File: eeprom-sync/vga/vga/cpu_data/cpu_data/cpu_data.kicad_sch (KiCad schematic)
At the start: 39 parts, among them J1 Conn_02x06_Odd_Even, J10 Conn_01x03_Female, J12 Conn_02x05_Odd_Even, J2 Conn_01x04_Male, J3 Conn_01x04_Female, J4 Conn_01x15_Female, J5 Conn_01x15_Female, J6 Conn_01x08_Female, J7 Conn_02x04_Odd_Even, J8 Conn_02x08_Odd_Even, J9 Conn_01x08_Female, Q1 Q_NMOS_GSD, U1 GAL22V10, U2 74HC14, U3 74LS02, U4 IDT7205L12JG, U5 74LS573

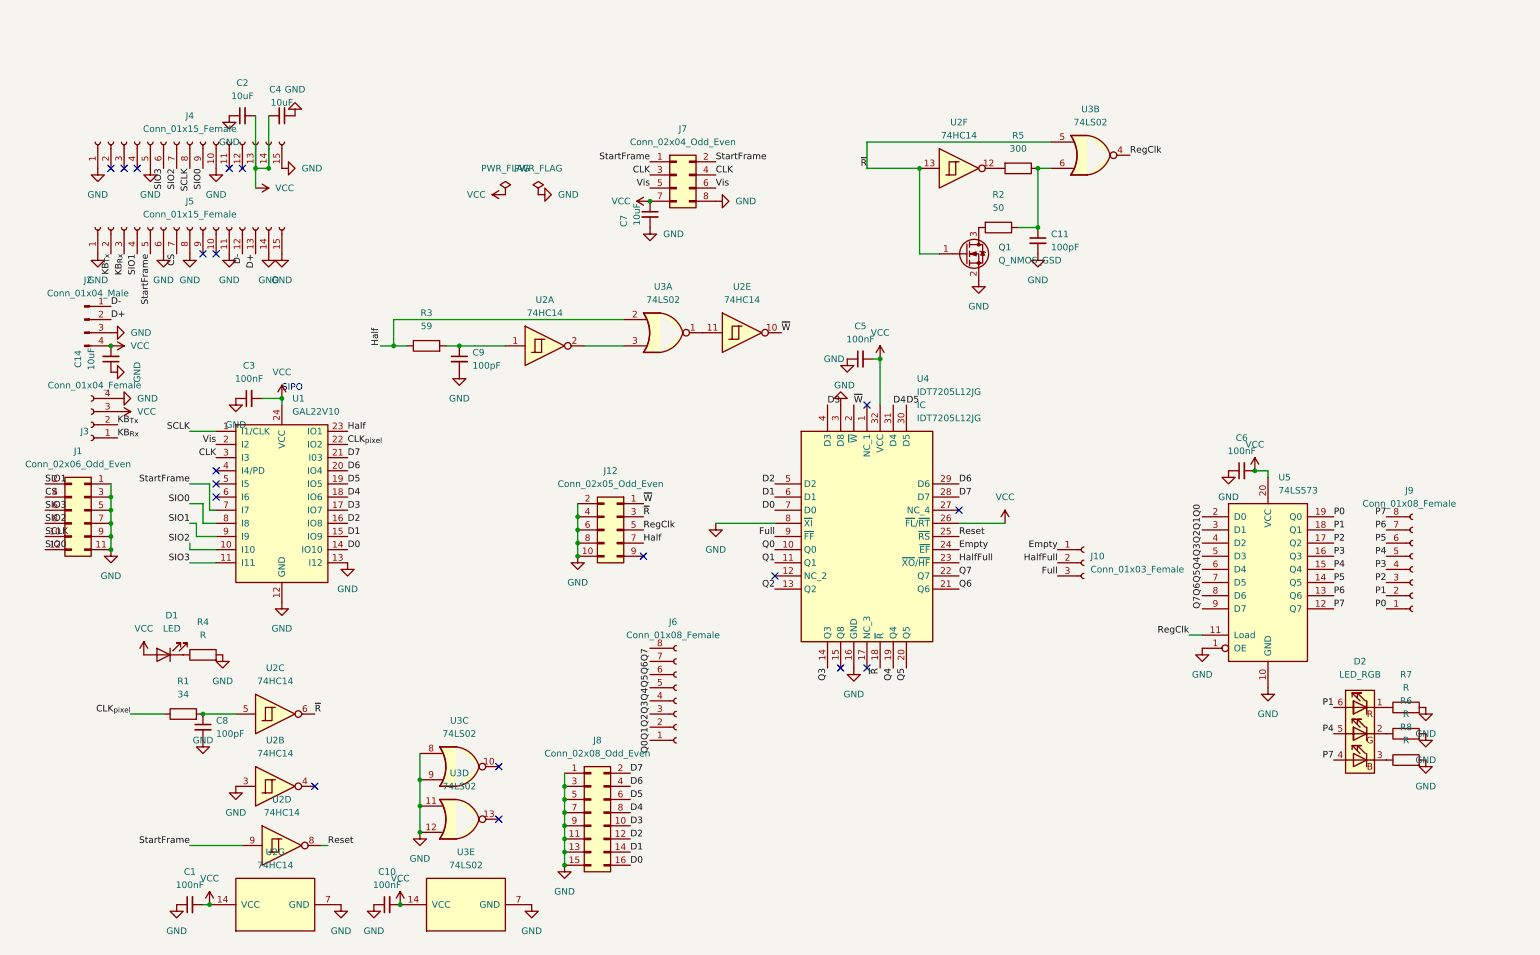
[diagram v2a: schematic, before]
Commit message: updating board to use clocked latches as the data mile markers instead of RC time circuits. Also adding a clock board breadboardable circuit module
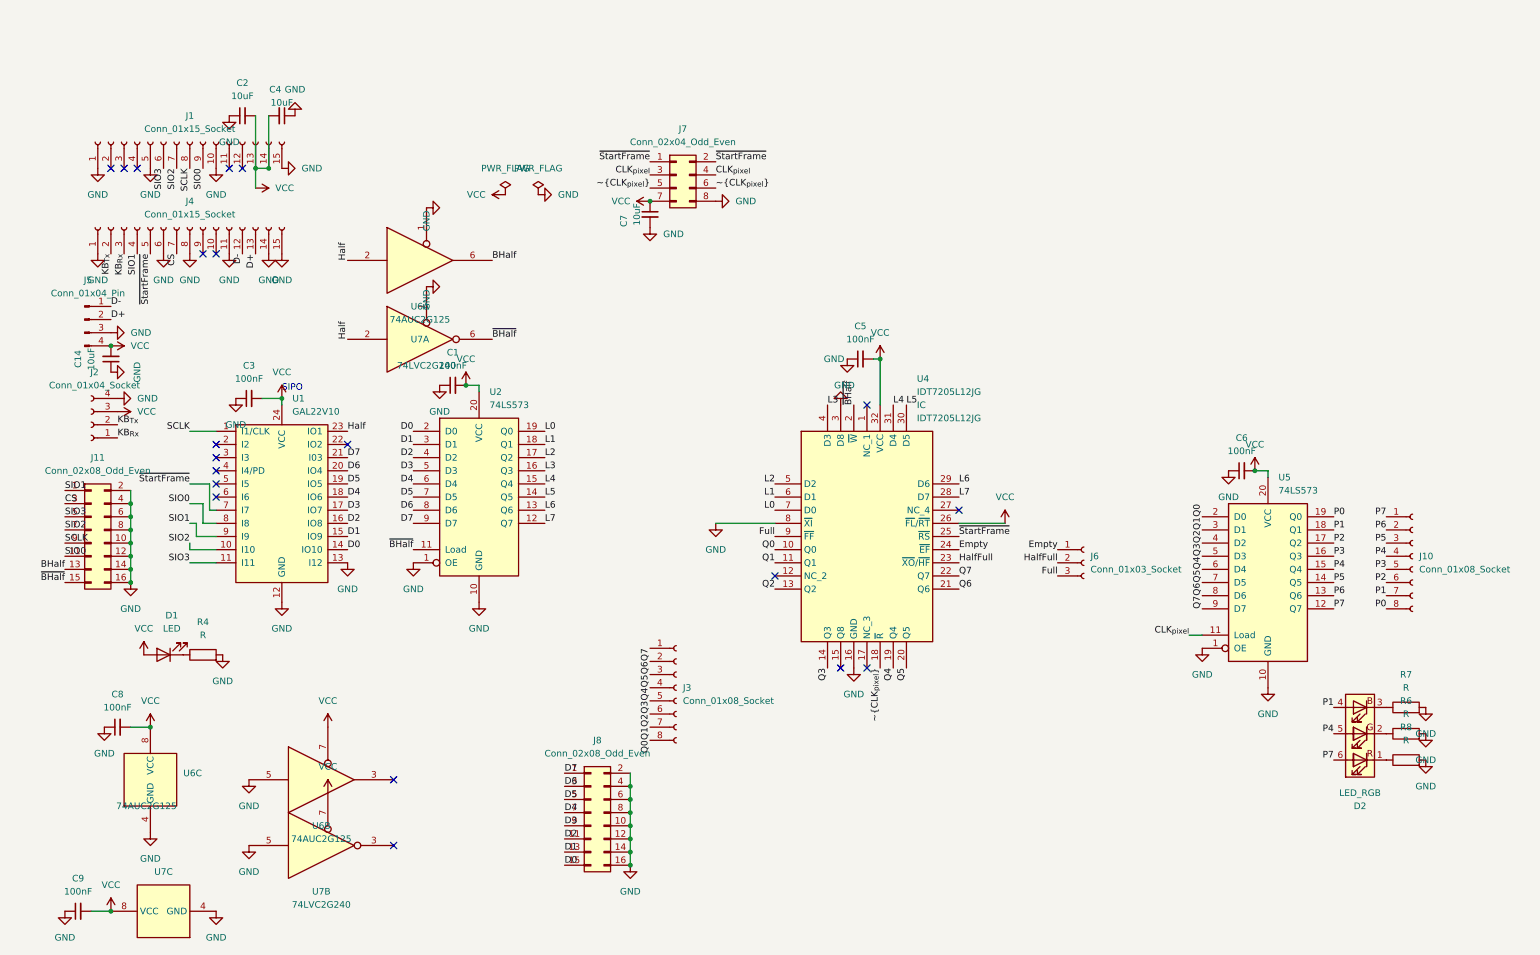
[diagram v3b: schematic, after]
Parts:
- removed C10: 100nF, Capacitor_SMD:C_0805_2012Metric_Pad1.18x1.45mm_HandSolder, symbol Device:C_Small
- removed C11: 100pF, Capacitor_SMD:C_0805_2012Metric_Pad1.18x1.45mm_HandSolder, symbol Device:C_Small
- removed J1: Conn_02x06_Odd_Even, Connector_PinHeader_2.54mm:PinHeader_2x06_P2.54mm_Vertical, symbol Connector_Generic:Conn_02x06_Odd_Even
- removed J10: Conn_01x03_Female, Connector_PinSocket_2.54mm:PinSocket_1x03_P2.54mm_Vertical, symbol Connector:Conn_01x03_Female
- removed J12: Conn_02x05_Odd_Even, Connector_PinHeader_2.54mm:PinHeader_2x05_P2.54mm_Vertical, symbol Connector_Generic:Conn_02x05_Odd_Even
- removed J2: Conn_01x04_Male, Connector_PinHeader_2.54mm:PinHeader_1x04_P2.54mm_Vertical, symbol Connector:Conn_01x04_Male
- removed J3: Conn_01x04_Female, Connector_PinSocket_2.54mm:PinSocket_1x04_P2.54mm_Vertical, symbol Connector:Conn_01x04_Female
- removed J4, J5: Conn_01x15_Female, Connector_PinSocket_2.54mm:PinSocket_1x15_P2.54mm_Vertical, symbol Connector:Conn_01x15_Female
- removed J6, J9: Conn_01x08_Female, Connector_PinSocket_2.54mm:PinSocket_1x08_P2.54mm_Vertical, symbol Connector:Conn_01x08_Female
- removed Q1: Q_NMOS_GSD, Package_TO_SOT_SMD:SOT-323_SC-70_Handsoldering, symbol Device:Q_NMOS_GSD
- removed R1: 34, Resistor_SMD:R_0805_2012Metric_Pad1.20x1.40mm_HandSolder, symbol Device:R
- removed R2: 50, Resistor_SMD:R_0805_2012Metric_Pad1.20x1.40mm_HandSolder, symbol Device:R
- removed R3: 59, Resistor_SMD:R_0805_2012Metric_Pad1.20x1.40mm_HandSolder, symbol Device:R
- removed R5: 300, Resistor_SMD:R_0805_2012Metric_Pad1.20x1.40mm_HandSolder, symbol Device:R
- removed U2: 74HC14, Package_SO:SOIC-14_3.9x8.7mm_P1.27mm, symbol 74xx:74HC14
- removed U3: 74LS02, Package_SO:SOIC-14_3.9x8.7mm_P1.27mm, symbol 74xx:74LS02
- added J1, J4: Conn_01x15_Socket, Connector_PinSocket_2.54mm:PinSocket_1x15_P2.54mm_Vertical, symbol Connector:Conn_01x15_Socket
- added J10: Conn_01x08_Socket, Connector_PinSocket_2.54mm:PinSocket_1x08_P2.54mm_Vertical, symbol Connector:Conn_01x08_Socket
- added J11: Conn_02x08_Odd_Even, Connector_PinHeader_2.54mm:PinHeader_2x08_P2.54mm_Vertical, symbol Connector_Generic:Conn_02x08_Odd_Even
- added J2: Conn_01x04_Socket, Connector_PinSocket_2.54mm:PinSocket_1x04_P2.54mm_Vertical, symbol Connector:Conn_01x04_Socket
- added J3: Conn_01x08_Socket, Connector_PinHeader_2.54mm:PinHeader_1x08_P2.54mm_Vertical, symbol Connector:Conn_01x08_Socket
- added J5: Conn_01x04_Pin, Connector_PinHeader_2.54mm:PinHeader_1x04_P2.54mm_Vertical, symbol Connector:Conn_01x04_Pin
- added J6: Conn_01x03_Socket, Connector_PinSocket_2.54mm:PinSocket_1x03_P2.54mm_Vertical, symbol Connector:Conn_01x03_Socket
- added U2: 74LS573, Package_SO:SOIC-20W_7.5x15.4mm_P1.27mm, symbol 74xx:74LS573
- added U6: 74AUC2G125, Package_SO:TSSOP-8_3x3mm_P0.65mm, symbol 74xGxx:74AUC2G125
- added U7: 74LVC2G240, Package_SO:TSSOP-8_3x3mm_P0.65mm, symbol 74xGxx:74LVC2G240
- C1: footprint Capacitor_SMD:C_0805_2012Metric_Pad1.18x1.45mm_HandSolder -> plcc32:plcc32-socket; Pruduct (none) -> https://www.mouser.com/ProductDetail/Samsung-Electro-Mechan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
- C8: value 100pF -> 100nF
- C9: value 100pF -> 100nF; Product https://www.mouser.com/ProductDetail/Samsung-Electro-Mechan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 -> (none)
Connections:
- net RegClk is gone; now on net CLK_{pixel}: U5.11 (Load)
- net StartFrame is gone; now on net ~{StartFrame}: J7.1 (Pin_1), J7.2 (Pin_2), U1.7 (I7)
- net ~{R} is gone; now on net ~{CLK_{pixel}}: U4.18 (~{R})
- net CLK_{pixel}: now also J7.3 (Pin_3), J7.4 (Pin_4); no longer U1.22 (IO2)
- net CS: now also J11.3 (Pin_3), J4.7 (Pin_7)
- net D+: now also J4.13 (Pin_13), J5.2 (Pin_2)
- net D-: now also J4.12 (Pin_12), J5.1 (Pin_1)
- net D0: now also J8.15 (Pin_15), U2.2 (D0); no longer J8.16 (Pin_16), U4.7 (D0)
- net D1: now also J8.13 (Pin_13), U2.3 (D1); no longer J8.14 (Pin_14), U4.6 (D1)
- net D2: now also J8.11 (Pin_11), U2.4 (D2); no longer J8.12 (Pin_12), U4.5 (D2)
- net D3: now also J8.9 (Pin_9), U2.5 (D3); no longer J8.10 (Pin_10), U4.4 (D3)
- net D4: now also J8.7 (Pin_7), U2.6 (D4); no longer J8.8 (Pin_8), U4.31 (D4)
- net D5: now also J8.5 (Pin_5), U2.7 (D5); no longer J8.6 (Pin_6), U4.30 (D5)
- net D6: now also J8.3 (Pin_3), U2.8 (D6); no longer J8.4 (Pin_4), U4.29 (D6)
- net D7: now also J8.1 (Pin_1), U2.9 (D7); no longer J8.2 (Pin_2), U4.28 (D7)
- net Empty: now also J6.1 (Pin_1)
- net Full: now also J6.3 (Pin_3)
- net GND: now also C8.1, C9.1, J8.10 (Pin_10), J8.12 (Pin_12), J8.14 (Pin_14), J8.16 (Pin_16), J8.2 (Pin_2), J8.4 (Pin_4), J8.6 (Pin_6), J8.8 (Pin_8), J1.1 (Pin_1), J1.10 (Pin_10), J1.15 (Pin_15), J1.5 (Pin_5), J11.10 (Pin_10), J11.12 (Pin_12), J11.14 (Pin_14), J11.16 (Pin_16), J11.2 (Pin_2), J11.4 (Pin_4), J11.6 (Pin_6), J11.8 (Pin_8), J2.4 (Pin_4), J4.1 (Pin_1), J4.11 (Pin_11), J4.14 (Pin_14), J4.15 (Pin_15), J4.6 (Pin_6), J4.8 (Pin_8), J5.3 (Pin_3), U2.1 (OE), U2.10 (GND), U6.1, U6.4 (GND), U6.5, U7.1, U7.4 (GND), U7.5; no longer C8.2, C9.2, J8.1 (Pin_1), J8.11 (Pin_11), J8.13 (Pin_13), J8.15 (Pin_15), J8.3 (Pin_3), J8.5 (Pin_5), J8.7 (Pin_7), J8.9 (Pin_9)
- net Half: now also U6.2, U7.2
- net HalfFull: now also J6.2 (Pin_2)
- net KB_{Rx}: now also J2.1 (Pin_1), J4.3 (Pin_3)
- net KB_{Tx}: now also J2.2 (Pin_2), J4.2 (Pin_2)
- net P0: now also J10.8 (Pin_8)
- net P1: now also D2.4 (BA), J10.7 (Pin_7); no longer D2.6 (RA)
- net P2: now also J10.6 (Pin_6)
- net P3: now also J10.5 (Pin_5)
- net P4: now also J10.4 (Pin_4)
- net P5: now also J10.3 (Pin_3)
- net P6: now also J10.2 (Pin_2)
- net P7: now also D2.6 (RA), J10.1 (Pin_1); no longer D2.4 (BA)
- net Q0: now also J3.8 (Pin_8)
- net Q1: now also J3.7 (Pin_7)
- net Q2: now also J3.6 (Pin_6)
- net Q3: now also J3.5 (Pin_5)
- net Q4: now also J3.4 (Pin_4)
- net Q5: now also J3.3 (Pin_3)
- net Q6: now also J3.2 (Pin_2)
- net Q7: now also J3.1 (Pin_1)
- net SCLK: now also J1.8 (Pin_8), J11.9 (Pin_9)
- net SIO0: now also J1.9 (Pin_9), J11.11 (Pin_11)
- net SIO1: now also J11.1 (Pin_1), J4.4 (Pin_4)
- net SIO2: now also J1.7 (Pin_7), J11.7 (Pin_7)
- net SIO3: now also J1.6 (Pin_6), J11.5 (Pin_5)
- net VCC: now also C8.2, C9.2, J1.13 (Pin_13), J1.14 (Pin_14), J2.3 (Pin_3), J5.4 (Pin_4), U2.20 (VCC), U6.7, U6.8 (VCC), U7.7, U7.8 (VCC)
- net at R8.1: now also D2.1 (RK); no longer D2.3 (BK)
- net at R7.1: now also D2.3 (BK); no longer D2.1 (RK)
- removed net CLK: J7.3 (Pin_3), J7.4 (Pin_4), U1.3 (I3)
- net Reset renamed ~{StartFrame}
- net ~{StartFrame}: now also J4.5 (Pin_5)
- net Vis renamed ~{CLK_{pixel}}
- net ~{CLK_{pixel}}: no longer U1.2 (I2)
- net ~{W} renamed ~{BHalf}
- net ~{BHalf}: now also J11.15 (Pin_15), U2.11 (Load), U7.6
- new net BHalf: J11.13 (Pin_13), U6.6
- new net L0: U2.19 (Q0), U4.7 (D0)
- new net L1: U2.18 (Q1), U4.6 (D1)
- new net L2: U2.17 (Q2), U4.5 (D2)
- new net L3: U2.16 (Q3), U4.4 (D3)
- new net L4: U2.15 (Q4), U4.31 (D4)
- new net L5: U2.14 (Q5), U4.30 (D5)
- new net L6: U2.13 (Q6), U4.29 (D6)
- new net L7: U2.12 (Q7), U4.28 (D7)
- no-connect marks 19 -> 20
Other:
- moved on the sheet: D2

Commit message: final board
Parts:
- removed C1: 100nF, plcc32:plcc32-socket, symbol Device:C_Small
- removed C8, C9: 100nF, Capacitor_SMD:C_0805_2012Metric_Pad1.18x1.45mm_HandSolder, symbol Device:C_Small
- removed J11: Conn_02x08_Odd_Even, Connector_PinHeader_2.54mm:PinHeader_2x08_P2.54mm_Vertical, symbol Connector_Generic:Conn_02x08_Odd_Even
- removed U2, U5: 74LS573, Package_SO:SOIC-20W_7.5x15.4mm_P1.27mm, symbol 74xx:74LS573
- removed U6: 74AUC2G125, Package_SO:TSSOP-8_3x3mm_P0.65mm, symbol 74xGxx:74AUC2G125
- removed U7: 74LVC2G240, Package_SO:TSSOP-8_3x3mm_P0.65mm, symbol 74xGxx:74LVC2G240
- added C10: 100nF, Capacitor_SMD:C_0805_2012Metric_Pad1.18x1.45mm_HandSolder, symbol Device:C_Small
- added J9: Conn_02x07_Odd_Even, Connector_PinHeader_2.54mm:PinHeader_2x07_P2.54mm_Vertical, symbol Connector_Generic:Conn_02x07_Odd_Even
- added U2: 74HCT574, Package_SO:SOIC-20W_7.5x12.8mm_P1.27mm, symbol 74xx:74HCT574
- added U3: 74AHCT244, Package_SO:TSSOP-20_4.4x6.5mm_P0.65mm, symbol 74xx:74AHCT244
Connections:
- net CLK_{pixel} is gone; now on net Clk: J7.3 (Pin_3), J7.4 (Pin_4)
- net ~{BHalf} is gone; now on net Half: U4.2 (~{W})
- net CS: now also J9.3 (Pin_3)
- net D0: now also U3.2 (1A0)
- net D1: now also U3.4 (1A1)
- net D2: now also U3.6 (1A2)
- net D3: now also U3.8 (1A3)
- net D4: now also U3.17 (2A0)
- net D5: now also U3.15 (2A1)
- net D6: now also U3.13 (2A2)
- net D7: now also U3.11 (2A3)
- net GND: now also C10.1, J9.10 (Pin_10), J9.12 (Pin_12), J9.14 (Pin_14), J9.2 (Pin_2), J9.4 (Pin_4), J9.6 (Pin_6), J9.8 (Pin_8), U2.1 (OE), U2.10 (GND), U3.1 (1OE), U3.10 (GND), U3.19 (2OE)
- net Half: now also J9.13 (Pin_13)
- net L0: now also U3.18 (1Y0)
- net L1: now also U3.16 (1Y1)
- net L2: now also U3.14 (1Y2)
- net L3: now also U3.12 (1Y3)
- net L4: now also U3.3 (2Y0)
- net L5: now also U3.5 (2Y1)
- net L6: now also U3.7 (2Y2)
- net L7: now also U3.9 (2Y3)
- net P0: now also U2.19 (Q0)
- net P1: now also U2.18 (Q1)
- net P2: now also U2.17 (Q2)
- net P3: now also U2.16 (Q3)
- net P4: now also U2.15 (Q4)
- net P5: now also U2.14 (Q5)
- net P6: now also U2.13 (Q6)
- net P7: now also U2.12 (Q7)
- net Q0: now also U2.2 (D0)
- net Q1: now also U2.3 (D1)
- net Q2: now also U2.4 (D2)
- net Q3: now also U2.5 (D3)
- net Q4: now also U2.6 (D4)
- net Q5: now also U2.7 (D5)
- net Q6: now also U2.8 (D6)
- net Q7: now also U2.9 (D7)
- net SCLK: now also J9.9 (Pin_9)
- net SIO0: now also J9.11 (Pin_11)
- net SIO1: now also J9.1 (Pin_1)
- net SIO2: now also J9.7 (Pin_7)
- net SIO3: now also J9.5 (Pin_5)
- net VCC: now also C10.2, U2.20 (VCC), U3.20 (VCC)
- net Vis: now reaches U1.2 (I2)
- net Vis: now also J7.5 (Pin_5), J7.6 (Pin_6)
- net Clk_{pixel}: now reaches U1.22 (IO2)
- net Clk_{pixel}: now also U4.18 (~{R}), U2.11 (Cp)
- net Clk: now reaches U1.3 (I3)
- removed net ~{CLK_{pixel}}: J7.5 (Pin_5), J7.6 (Pin_6), U4.18 (~{R})
- no-connect marks 20 -> 15
